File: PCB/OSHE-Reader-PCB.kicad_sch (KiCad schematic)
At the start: 2 parts

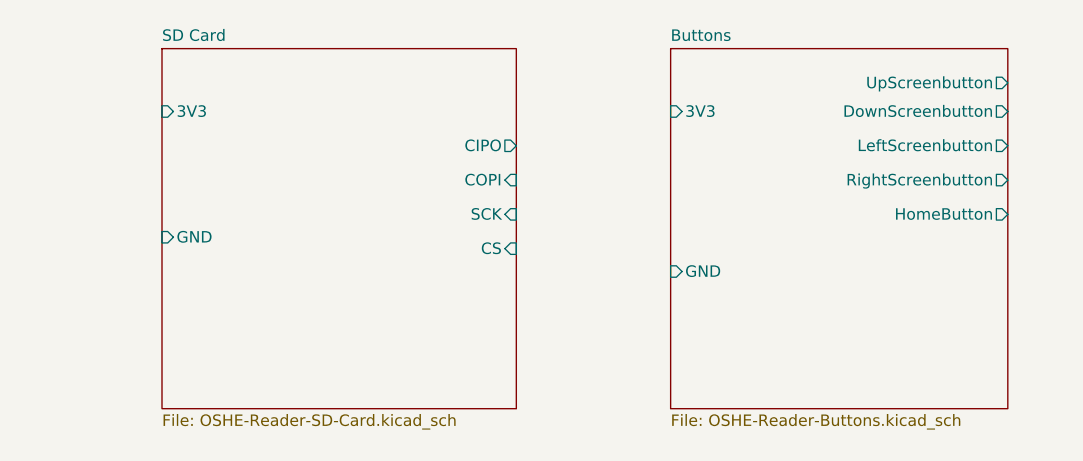
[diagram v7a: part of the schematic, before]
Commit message: Updates reader display connector
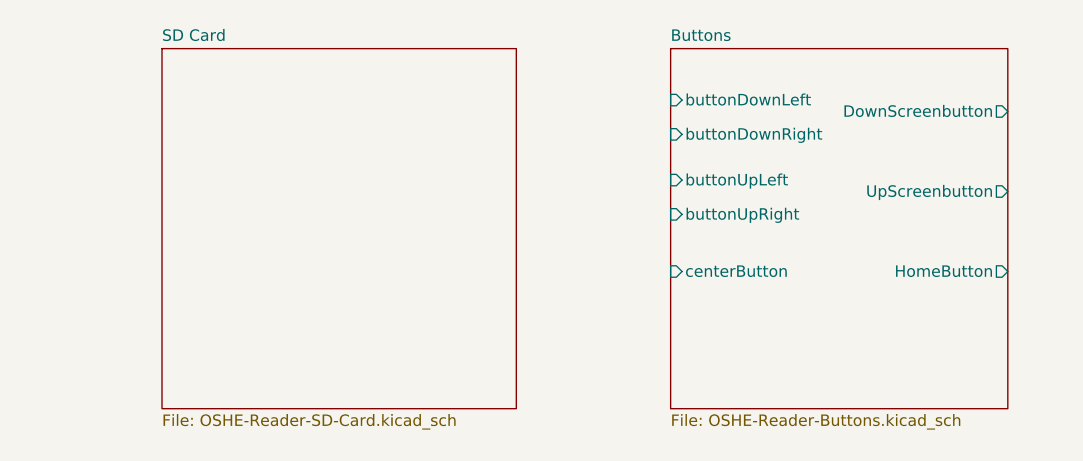
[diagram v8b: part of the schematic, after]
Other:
- sheet Buttons ports: added buttonDownLeft, buttonDownRight, buttonUpLeft, buttonUpRight, centerButton; removed 3V3, GND, LeftScreenbutton, RightScreenbutton
- sheet SD Card ports: added none; removed 3V3, CIPO, COPI, CS, GND, SCK
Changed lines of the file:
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@@
+			)
+		)
+		(pin "buttonDownLeft" input
+			(at 228.6 39.37 180)
+			(effects
+				(font
+					(size 1.27 1.27)
+				)
+				(justify left)
+			)
+		)
+		(pin "buttonUpLeft" input
+			(at 228.6 48.26 180)
+			(effects
+				(font
+					(size 1.27 1.27)
+				)
+				(justify left)
+			)
+		)
+		(pin "centerButton" input
+			(at 228.6 58.42 180)
+			(effects
+				(font
+					(size 1.27 1.27)
+				)
+				(justify left)
+			)
+		)
+		(pin "buttonDownRight" input
+			(at 228.6 43.18 180)
+			(effects
+				(font
+					(size 1.27 1.27)
+				)
+				(justify left)
+			)
+		)
+		(pin "buttonUpRight" input
+			(at 228.6 52.07 180)
+			(effects
+				(font
+					(size 1.27 1.27)
+				)
+				(justify left)
 			)
 		)
@@
 		)
 		(pin "HomeButton" output
-			(at 266.065 52.07 0)
+			(at 266.065 58.42 0)
 			(effects
 				(font
@@
 		)
 		(pin "UpScreenbutton" output
-			(at 266.065 37.465 0)
-			(effects
-				(font
-					(size 1.27 1.27)
-				)
-				(justify right)
-			)
-		)
-		(pin "GND" input
-			(at 228.6 58.42 180)
-			(effects
-				(font
-					(size 1.27 1.27)
-				)
-				(justify left)
-			)
-		)
-		(pin "3V3" input
-			(at 228.6 40.64 180)
-			(effects
-				(font
-					(size 1.27 1.27)
-				)
-				(justify left)
-			)
-		)
-		(pin "LeftScreenbutton" output
-			(at 266.065 44.45 0)
-			(effects
-				(font
-					(size 1.27 1.27)
-				)
-				(justify right)
-			)
-		)
-		(pin "RightScreenbutton" output
-			(at 266.065 48.26 0)
+			(at 266.065 49.53 0)
 			(effects
 				(font
@@
 			)
 		)
-		(pin "3V3" input
-			(at 172.085 40.64 180)
-			(effects
-				(font
-					(size 1.27 1.27)
-				)
-				(justify left)
-			)
-		)
-		(pin "CS" input
-			(at 211.455 55.88 0)
-			(effects
-				(font
-					(size 1.27 1.27)
-				)
-				(justify right)
-			)
-		)
-		(pin "GND" input
-			(at 172.085 54.61 180)
-			(effects
-				(font
-					(size 1.27 1.27)
-				)
-				(justify left)
-			)
-		)
-		(pin "CIPO" output
-			(at 211.455 44.45 0)
-			(effects
-				(font
-					(size 1.27 1.27)
-				)
-				(justify right)
-			)
-		)
-		(pin "COPI" input
-			(at 211.455 48.26 0)
-			(effects
-				(font
-					(size 1.27 1.27)
-				)
-				(justify right)
-			)
-		)
-		(pin "SCK" input
-			(at 211.455 52.07 0)
-			(effects
-				(font
-					(size 1.27 1.27)
-				)
-				(justify right)
-			)
-		)
